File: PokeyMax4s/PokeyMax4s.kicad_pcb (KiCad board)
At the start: 2 copper layers, 20.7 x 52.8 mm, 47 parts, among them J1 Audio_in, U1 TSV854IQ4T, U2 74CB3T16210, U3 MAX10, U4 74CB3T16210, X1 50MHz

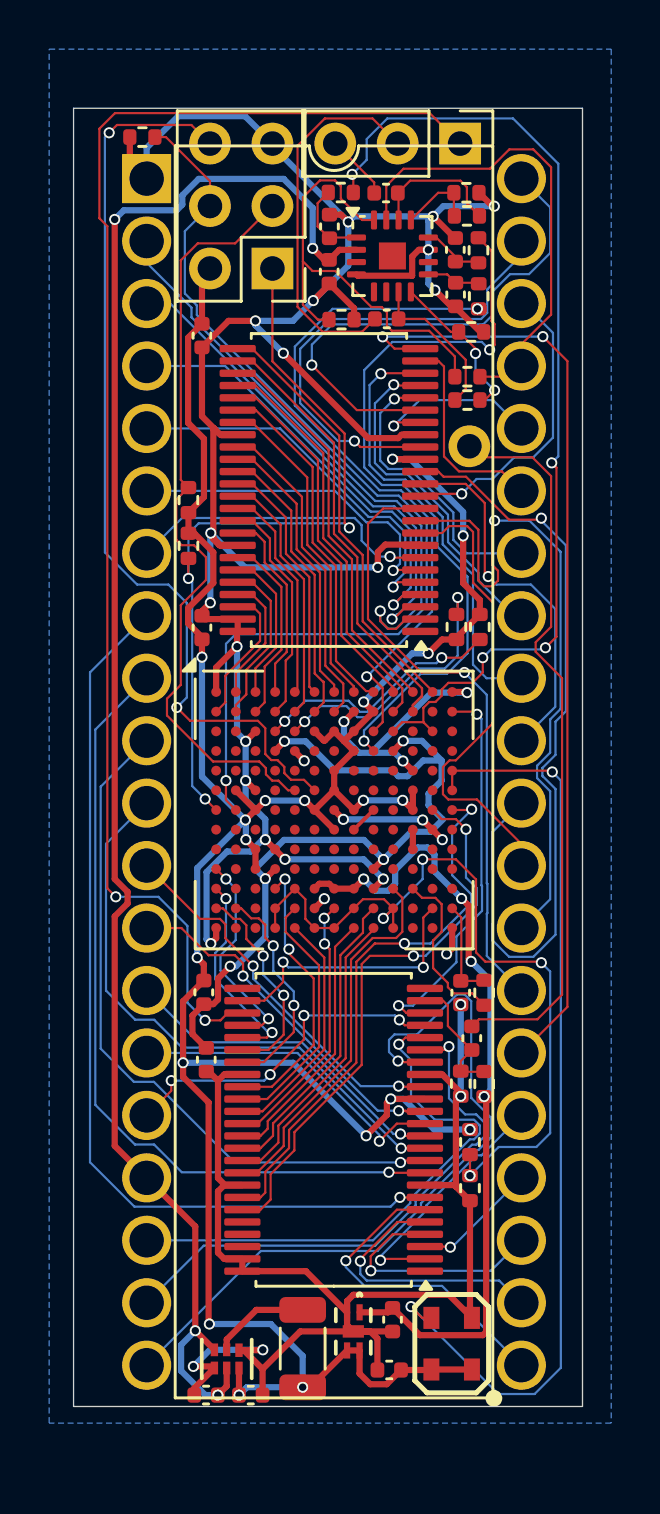
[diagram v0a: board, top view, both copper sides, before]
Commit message: Complete routing of Pokeymax 4s
Removed backup dirs from repo
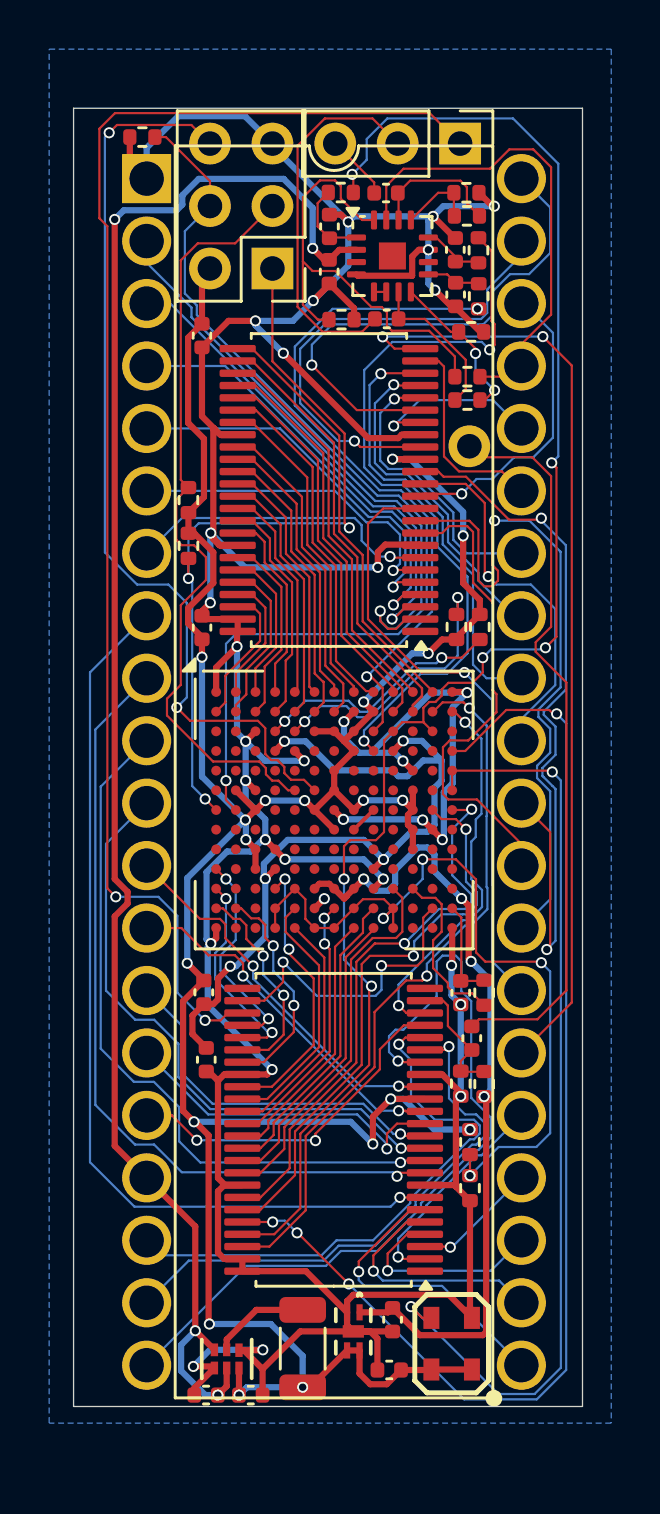
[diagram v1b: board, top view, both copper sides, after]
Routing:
- net LIN23: track 0.00 -> 48.5 mm, vias 0 -> 4
- net LIN20: track 0.00 -> 29.3 mm, vias 0 -> 2
- net AUD1: track 40.4 -> 65.7 mm, vias 4 -> 6
- net GND: track 177.8 -> 196.5 mm, vias 31 -> 32
- net ~{K3}: track 30.2 -> 33.1 mm
- net ~{CS0}: track 33.0 -> 31.4 mm, vias 1 -> 2
- net LINB9: track 11.1 -> 12.5 mm
- net ~{K0}: track 9.81 -> 8.49 mm
- net ~{KR1}: track 10.2 -> 9.08 mm
- net P0: track 13.8 -> 14.9 mm
- net ~{K1}: track 10.9 -> 9.85 mm
- net 3V3A: track 32.6 -> 31.7 mm
- net P4: track 28.4 -> 29.3 mm
- net P5: track 23.9 -> 24.7 mm
- net ~{K2}: track 13.1 -> 12.4 mm
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
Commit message: PokeyMax 4s silkscreen
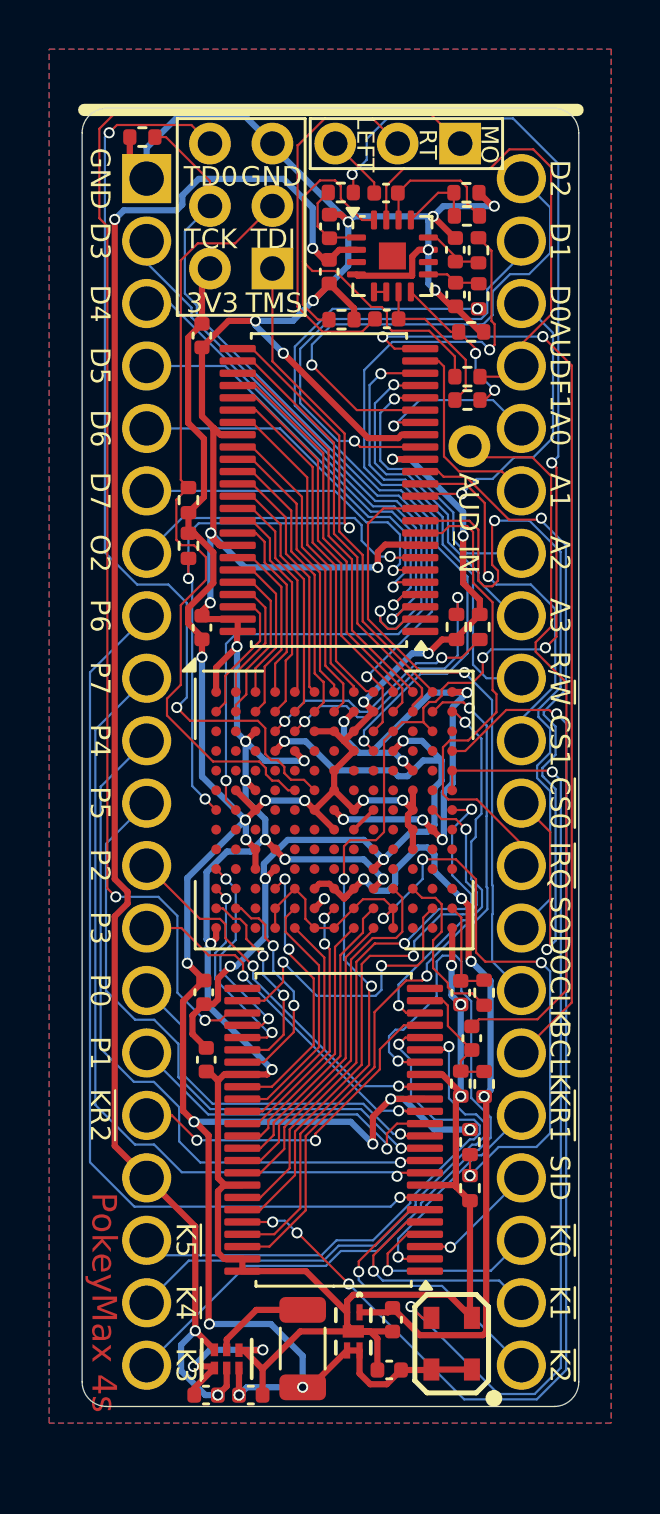
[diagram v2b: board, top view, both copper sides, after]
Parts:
- added REF**: KiCad-Logo2_5mm_SilkScreen, Symbol:KiCad-Logo2_5mm_SilkScreen, B.Cu at (151.3, 86.5)
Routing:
- added copper zone on F.Cu, net GND
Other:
- board size 20.7 x 52.8 mm -> 20.2 x 52.8 mm
- board text added: "3V3"
- board text added: "A0"
- board text added: "A1"
- board text added: "A2"
- board text added: "A3"
- board text added: "AUDF1"
- board text added: "AUD_IN"
- board text added: "BCLK"
- board text added: "CS1"
- board text added: "D0"
- board text added: "D1"
- board text added: "D2"
- board text added: "D3"
- board text added: "D4"
- board text added: "D5"
- board text added: "D6"
- board text added: "D7"
- board text added: "GND"
- board text added: "LEFT"
- board text added: "MO"
- board text added: "O2"
- board text added: "OCLK"
- board text added: "Original design by Foft https://forums.atariage.com/profile/8458-foft/ 2024 Redrawn by ScreamingAtTheRadio https://github.com/bleroy/pokeymax/tree/main/PokeyMax4s"
- board text added: "P0"
- board text added: "P1"
- board text added: "P2"
- board text added: "P3"
- board text added: "P4"
- board text added: "P5"
- board text added: "P6"
- board text added: "P7"
- board text added: "PokeyMax 4s"
- board text added: "R/~{W}"
- board text added: "RT"
- board text added: "SID"
- board text added: "SOD"
- board text added: "TCK"
- board text added: "TD0"
- board text added: "TDI"
- board text added: "TMS"
- board text added: "~{CS0}"
- board text added: "~{IRQ}"
- board text added: "~{K0}"
- board text added: "~{K1}"
- board text added: "~{K2}"
- board text added: "~{K3}"
- board text added: "~{K4}"
- board text added: "~{K5}"
- board text added: "~{KR1}"
- board text added: "~{KR2}"

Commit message: PokeyMax 4s fabrication files
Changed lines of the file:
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@@
 		(sheetname "ADC")
 		(sheetfile "ADC.kicad_sch")
-		(attr through_hole)
+		(attr through_hole exclude_from_bom)
 		(fp_text user "${REFERENCE}"
 			(at 0 0 90)
@@
 		(sheetname "Audio filter")
 		(sheetfile "Audio_filter.kicad_sch")
-		(attr through_hole)
+		(attr through_hole exclude_from_bom)
 		(fp_line
 			(start -1.016 6.096)
@@
 		)
 		(fp_line
+			(start 1.016 -1.3272)
+			(end 1.016 6.096)
+			(stroke
+				(width 0.12)
+				(type solid)
+			)
+			(layer "F.SilkS")
+		)
+		(fp_line
 			(start -1.016 -1.7272)
 			(end -1.016 6.096)
@@
 		(fp_line
 			(start -1.016 -1.7272)
-			(end 1.016 -1.7272)
+			(end 0.616 -1.7272)
 			(stroke
 				(width 0.12)
@@
 		)
 		(fp_line
-			(start 1.016 -1.7272)
-			(end 1.016 6.096)
+			(start 0.616 -1.7272)
+			(end 1.016 -1.3272)
 			(stroke
 				(width 0.12)
-				(type solid)
+				(type default)
 			)
 			(layer "F.SilkS")
@@
 			)
 		)
-		(property "JLCPCB Rotation Offset" "90"
+		(property "JLCPCB Rotation Offset" "270"
 			(at 0 0 180)
 			(unlocked yes)

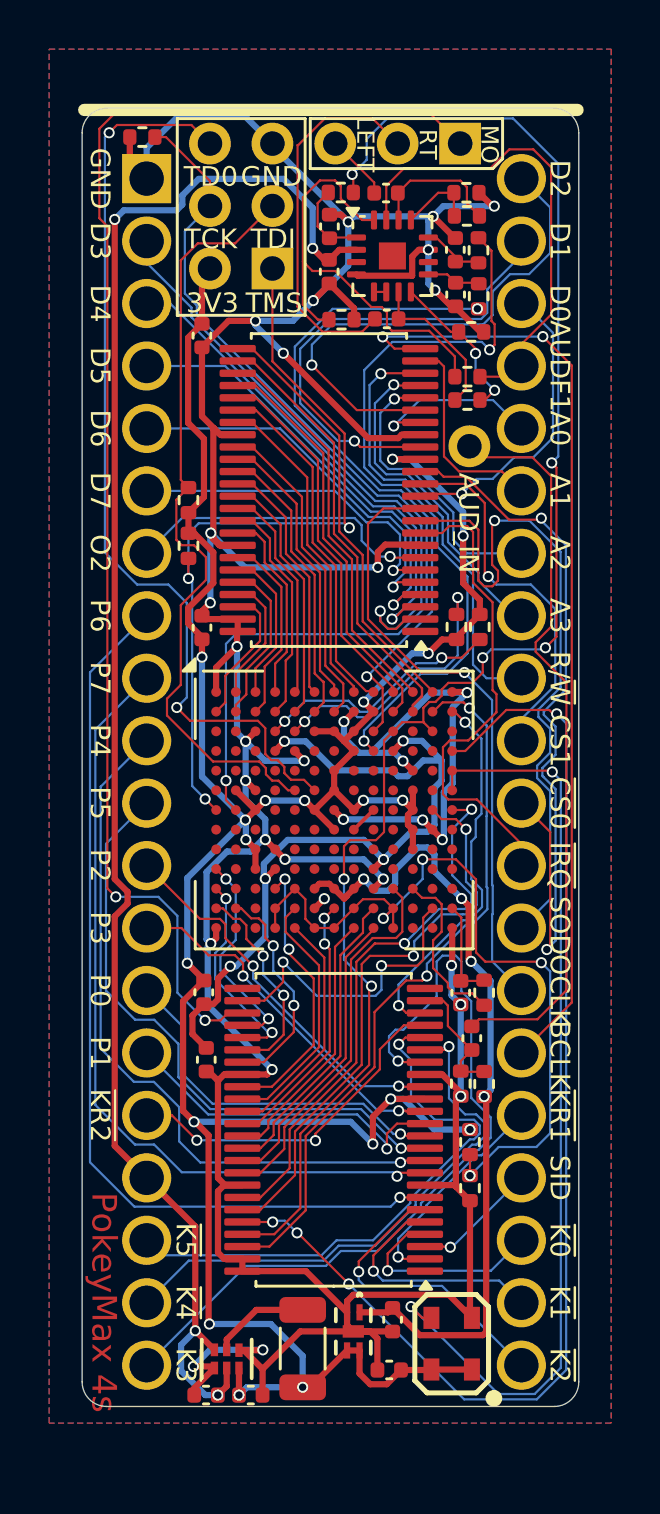
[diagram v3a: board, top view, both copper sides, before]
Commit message: Add A4 to PokeyMax 4s
Reroute accordingly
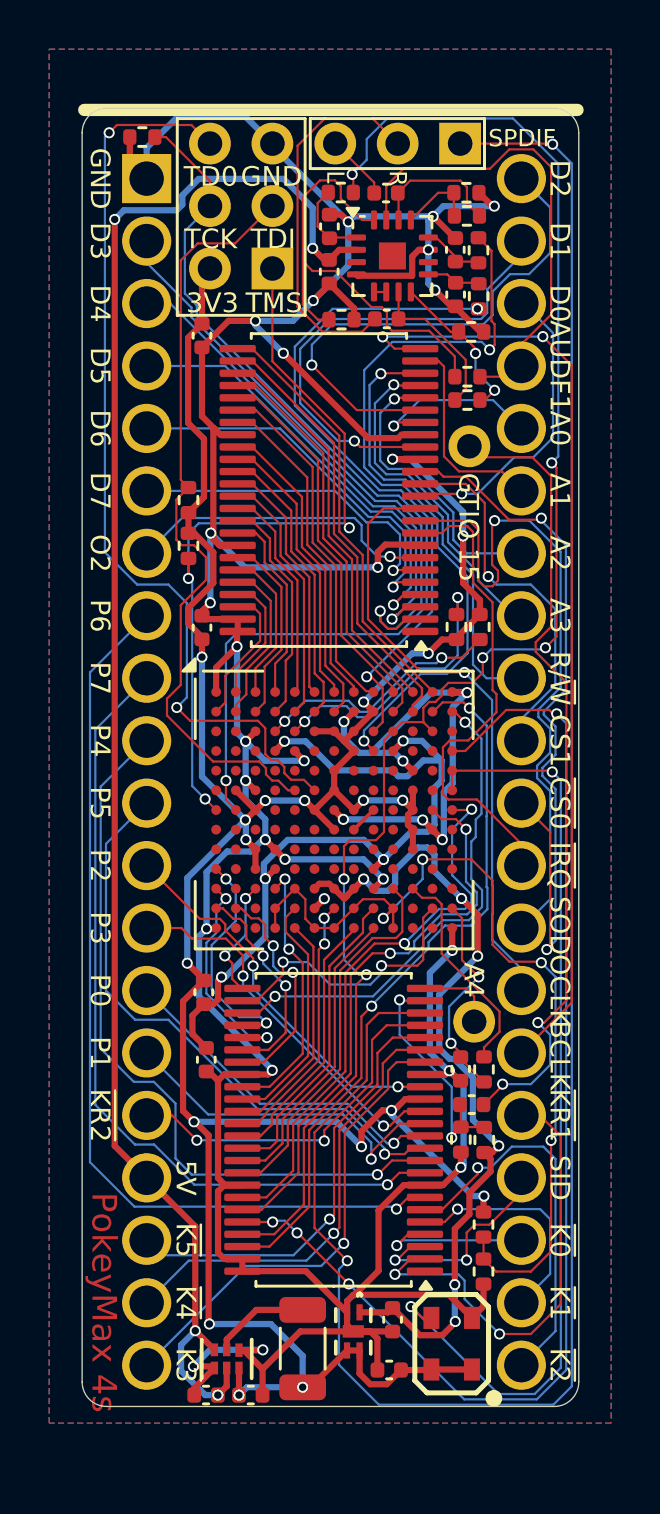
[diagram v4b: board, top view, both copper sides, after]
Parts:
- added J2: A4, Connector_PinHeader_2.54mm:PinHeader_1x01_P2.54mm_Vertical, F.Cu at (154.4, 115.8)
- J1: value Audio_in -> GTIA 15
- moved R7 3.43 mm to (154.8, 125.9)
- moved R6 3.40 mm to (154.8, 124.0)
- moved R10 3.12 mm to (154.8, 117.7), turned to -90 degrees
- moved C7 3.10 mm to (153.9, 117.7)
- moved C12 2.70 mm to (154.3, 119.1), turned to 0 degrees
- moved R8 2.28 mm to (153.9, 120.5)
- moved R9 2.28 mm to (154.9, 120.6)
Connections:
- net /Audio filter/AUDF3 renamed /Audio filter/RIGHT
- net /Audio filter/AUDF4 renamed /Audio filter/LEFT
- net AUD_IN renamed GTIA15
- AUD0 pad 1: LVLA21 -> DIGITAL_AUDIO_OUT
- U2 pad 22: LIN21 -> DIGITAL_AUDIO_OUT
- U2 pad 24: unconnected-(U2-2A10-Pad24) -> A4
- U2 pad 25: unconnected-(U2-2B10-Pad25) -> LINB18
- U2 pad 27: LVLA21 -> LIN21
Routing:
- net DIGITAL_AUDIO_OUT: track 0.00 -> 83.0 mm, vias 0 -> 2
- net LVLA21: track 55.6 -> 0.00 mm, vias 2 -> 0
- net ~{K3}: track 33.1 -> 19.5 mm
- net ~{KR1}: track 9.08 -> 17.6 mm, vias 1 -> 2
- net ~{K5}: track 23.1 -> 17.2 mm
- net LINB18: track 0.00 -> 4.86 mm, vias 0 -> 2
- net LVLB9: track 5.20 -> 9.92 mm, vias 0 -> 2
- net ADC_RX: track 4.00 -> 8.37 mm, vias 0 -> 2
- net LIN21: track 15.6 -> 19.8 mm
- net PTHRES: track 32.4 -> 36.5 mm
- net ~{K4}: track 22.2 -> 18.5 mm
- net ~{K2}: track 12.4 -> 15.7 mm
- net A4: track 0.00 -> 3.17 mm
- net GND: track 196.5 -> 199.6 mm
- net GTIA15: track 29.3 -> 32.2 mm, vias 0 -> 2
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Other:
- board text added: "5V"
- board text added: "A4"
- board text added: "D"
- board text added: "GTIO 15"
- board text added: "L"
- board text added: "Original design by Foft in 2024 https://forums.atariage.com/profile/8458-foft/ Redrawn by ScreamingAtTheRadio in 2024 https://github.com/bleroy/pokeymax/tree/main/PokeyMax4s"
- board text added: "R"
- board text added: "SPDIF"
- board text removed: "AUD_IN"
- board text removed: "LEFT"
- board text removed: "MO"
- board text removed: "Original design by Foft https://forums.atariage.com/profile/8458-foft/ 2024 Redrawn by ScreamingAtTheRadio https://github.com/bleroy/pokeymax/tree/main/PokeyMax4s"
- board text removed: "RT"

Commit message: Last adjustments to 4s
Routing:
- net AUD4: track 30.9 -> 36.8 mm
- net /FPGA/OSC_CLOCK: track 38.3 -> 33.1 mm
- net D1: track 19.0 -> 15.3 mm
- net D2: track 21.3 -> 18.1 mm
- net ~{KR1}: track 17.6 -> 14.6 mm
- net PTHRES: track 36.5 -> 33.8 mm
- net DIGITAL_AUDIO_OUT: track 83.0 -> 80.5 mm
- net 2V5: track 34.2 -> 32.1 mm, vias 6 -> 4
- net GND: track 199.6 -> 200.8 mm, vias 32 -> 31
- net 3V3: track 119.1 -> 120.2 mm
- net AUDF1: track 18.0 -> 18.9 mm
- net SID: track 7.77 -> 8.66 mm
- net D3: track 23.4 -> 24.3 mm
- net BCLK: track 38.7 -> 39.6 mm
- net ~{K1}: track 9.37 -> 8.50 mm
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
